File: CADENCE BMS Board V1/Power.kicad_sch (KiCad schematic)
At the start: 55 parts, among them J20 Conn_01x02, U1 TVS2200DRV, U2 LT8612, U3 LT3652IMSE#PBF

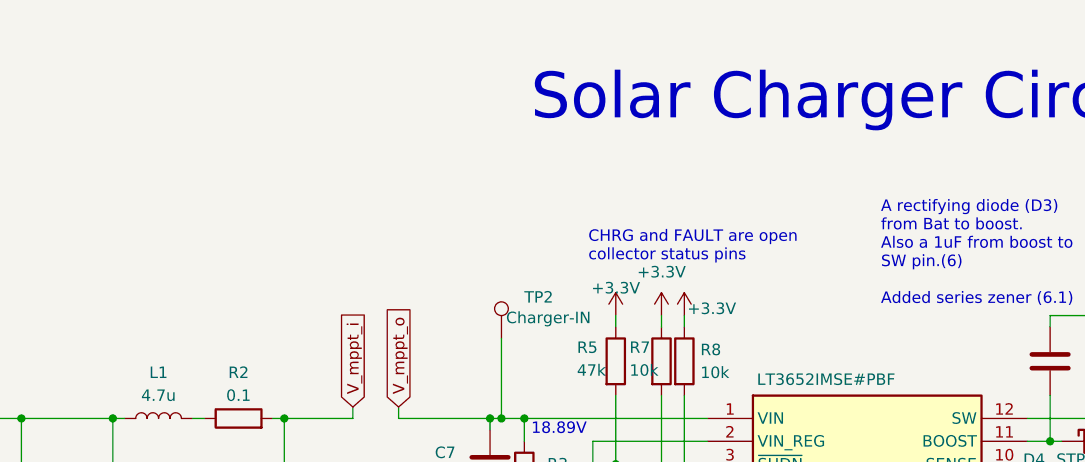
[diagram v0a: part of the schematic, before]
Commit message: Updates to Schematic
Found an error with power delivery USB-C and with the solar charger
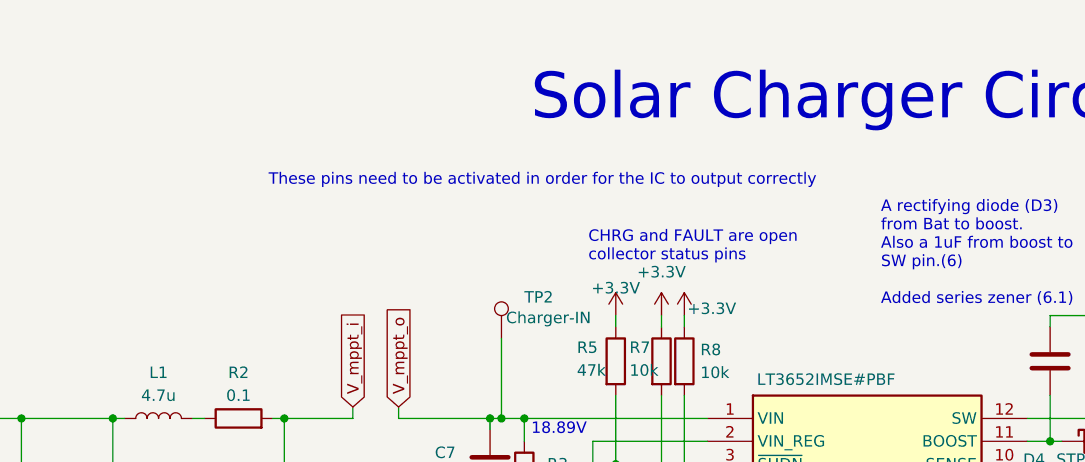
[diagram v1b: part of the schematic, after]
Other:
- note added: "These pins need to be activated in order for the IC to output correctly"
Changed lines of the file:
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@@
+		)
+	)
+	(text "These pins need to be activated in order for the IC to output correctly"
+		(exclude_from_sim no)
+		(at 200.152 32.004 0)
+		(effects
+			(font
+				(size 1.27 1.27)
+			)
 		)
 	)

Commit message: Troubleshooting Notes on things to change for next revision
Updates to the Solar charger to ensure it powers on and updates to USB-C schematic fixing an error with the pinouts of the p channel FETS
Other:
- note added: "Possibly connect SHDN into the Vin line for next revison if it works on testing"
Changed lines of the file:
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@@
+		)
+	)
+	(text "Possibly connect SHDN into the Vin line \nfor next revison if it works on testing"
+		(exclude_from_sim no)
+		(at 175.26 42.418 0)
+		(effects
+			(font
+				(size 1.27 1.27)
+			)
 		)
 	)

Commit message: Updates to component testing
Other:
- note added: "Possibly connect SHDN into the Vin line for next revison if it works on testing so the solar charger can power on without needing 3V3 buck to bypass inhibit system"
- note removed: "Possibly connect SHDN into the Vin line for next revison if it works on testing"
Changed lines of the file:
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@@
 		)
 	)
-	(text "Possibly connect SHDN into the Vin line \nfor next revison if it works on testing"
+	(text "Possibly connect SHDN into the Vin line \nfor next revison if it works on testing\nso the solar charger can power on without\nneeding 3V3 buck to bypass inhibit system"
 		(exclude_from_sim no)
-		(at 175.26 42.418 0)
+		(at 171.704 40.64 0)
 		(effects
 			(font
